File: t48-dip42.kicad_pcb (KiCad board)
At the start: 2 copper layers, 28.4 x 73.2 mm, 3 parts, among them J1 EPROM, J2 To T48 socket, J3 To T48 ribbon

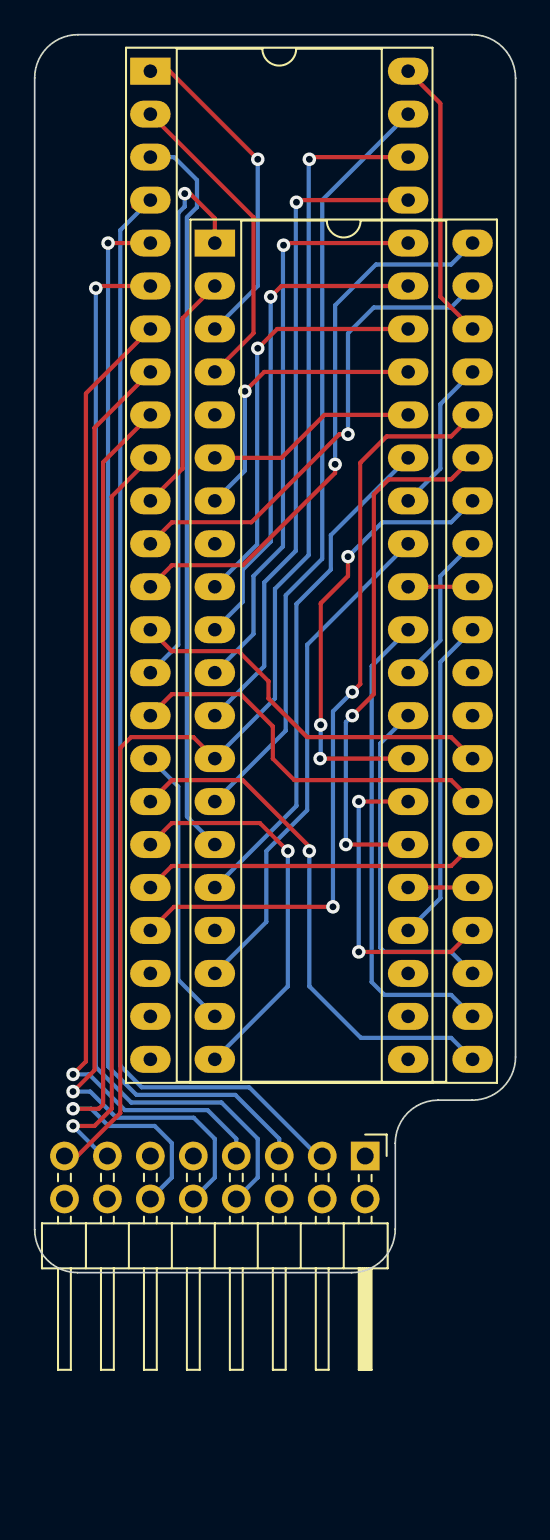
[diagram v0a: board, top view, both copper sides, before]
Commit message: v02: Move ribbon cable pins down to make room for test socket
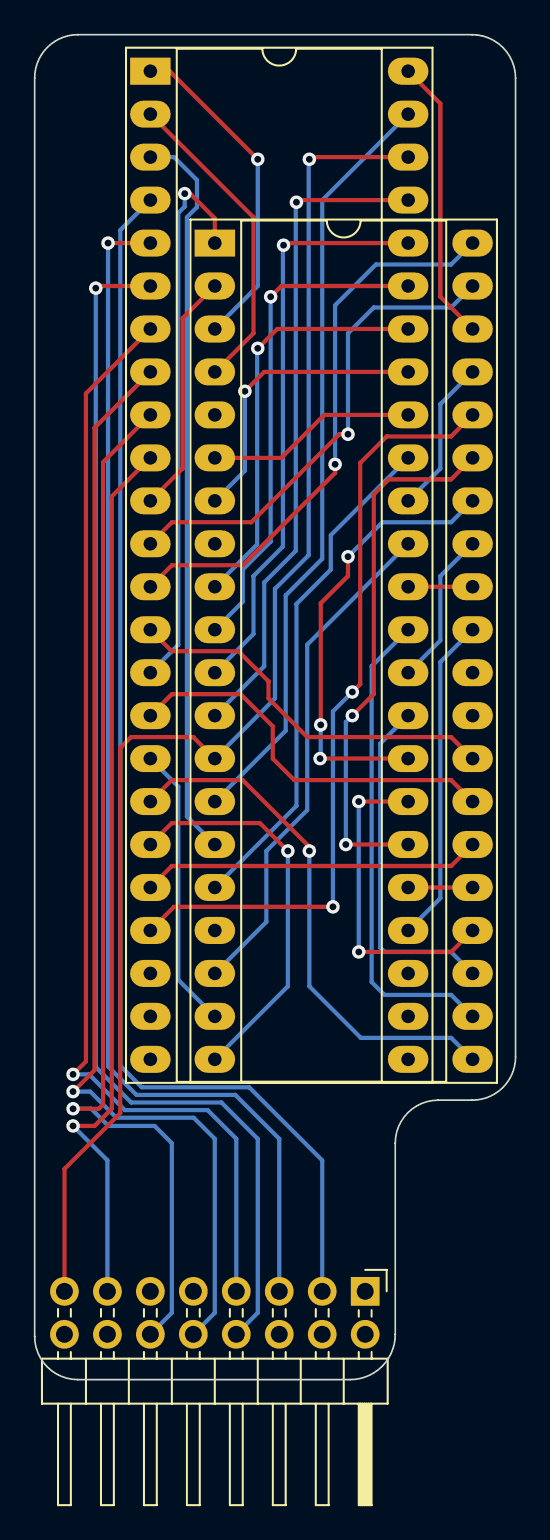
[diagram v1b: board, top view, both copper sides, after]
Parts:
- moved J3 8.00 mm to (156.0, 133.0)
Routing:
- net E09: track 54.3 -> 62.3 mm
- net E07: track 58.2 -> 66.2 mm
- net E06: track 64.7 -> 72.7 mm
- net E05: track 64.1 -> 72.1 mm
- net E08: track 58.1 -> 66.1 mm
- net E10: track 44.9 -> 52.8 mm
- net E04: track 67.2 -> 75.1 mm
- net E46: track 76.0 -> 83.5 mm
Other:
- board size 28.4 x 73.2 mm -> 28.4 x 79.5 mm

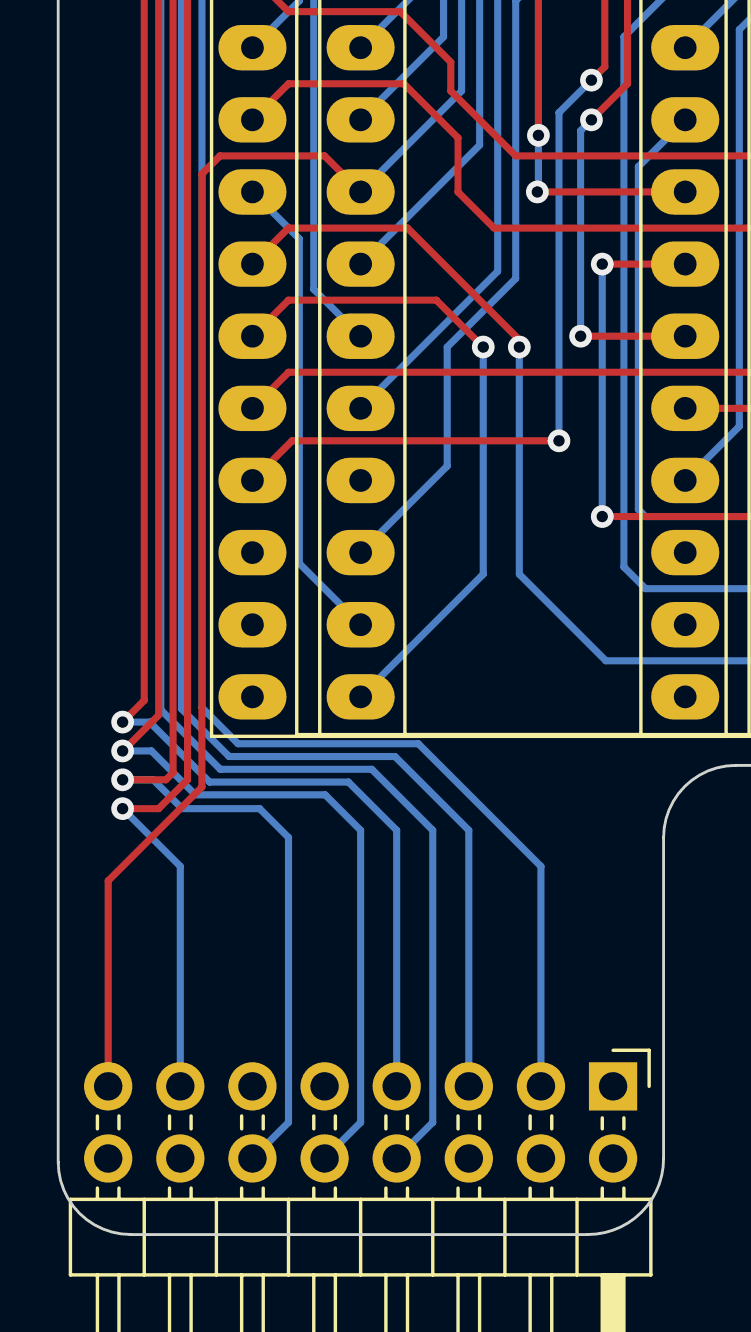
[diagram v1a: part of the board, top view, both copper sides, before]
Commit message: v03: Fix swapped upper/lower pins on ribbon cable
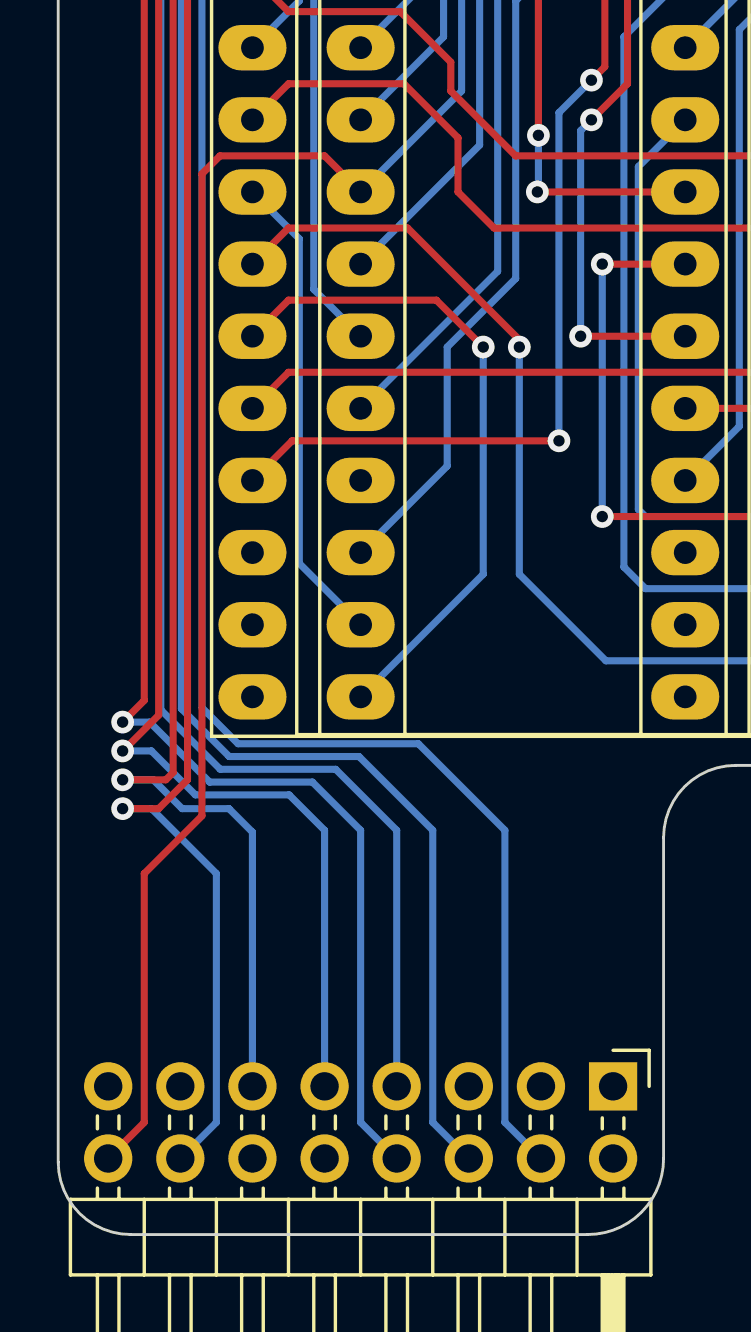
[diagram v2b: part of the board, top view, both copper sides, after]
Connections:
- J3 pad 10: E08 -> unconnected-(J3-Pin_10-Pad10)
- J3 pad 11: unconnected-(J3-Pin_11-Pad11) -> E09
- J3 pad 12: E09 -> unconnected-(J3-Pin_12-Pad12)
- J3 pad 13: E10 -> unconnected-(J3-Pin_13-Pad13)
- J3 pad 14: unconnected-(J3-Pin_14-Pad14) -> E10
- J3 pad 15: E46 -> unconnected-(J3-Pin_15-Pad15)
- J3 pad 16: unconnected-(J3-Pin_16-Pad16) -> E46
- J3 pad 3: E04 -> unconnected-(J3-Pin_3-Pad3)
- J3 pad 4: unconnected-(J3-Pin_4-Pad4) -> E04
- J3 pad 5: E05 -> unconnected-(J3-Pin_5-Pad5)
- J3 pad 6: unconnected-(J3-Pin_6-Pad6) -> E05
- J3 pad 7: E07 -> E06
- J3 pad 8: E06 -> E07
- J3 pad 9: unconnected-(J3-Pin_9-Pad9) -> E08
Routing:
- net E08: track 66.1 -> 61.7 mm
- net E06: track 72.7 -> 68.4 mm
- net E09: track 62.3 -> 58.1 mm
- net E10: track 52.8 -> 56.9 mm
- net E04: track 75.1 -> 77.6 mm
- net E46: track 83.5 -> 86.1 mm
- net E07: track 66.2 -> 68.0 mm
- net E05: track 72.1 -> 73.9 mm
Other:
- board text added: "v03"
